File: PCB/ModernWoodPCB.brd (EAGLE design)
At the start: 428.5 x 125 mm, 231 parts, among them Q2 FS8205, U1 ESP32-S3HOLE, U2 ME6211C33M5G

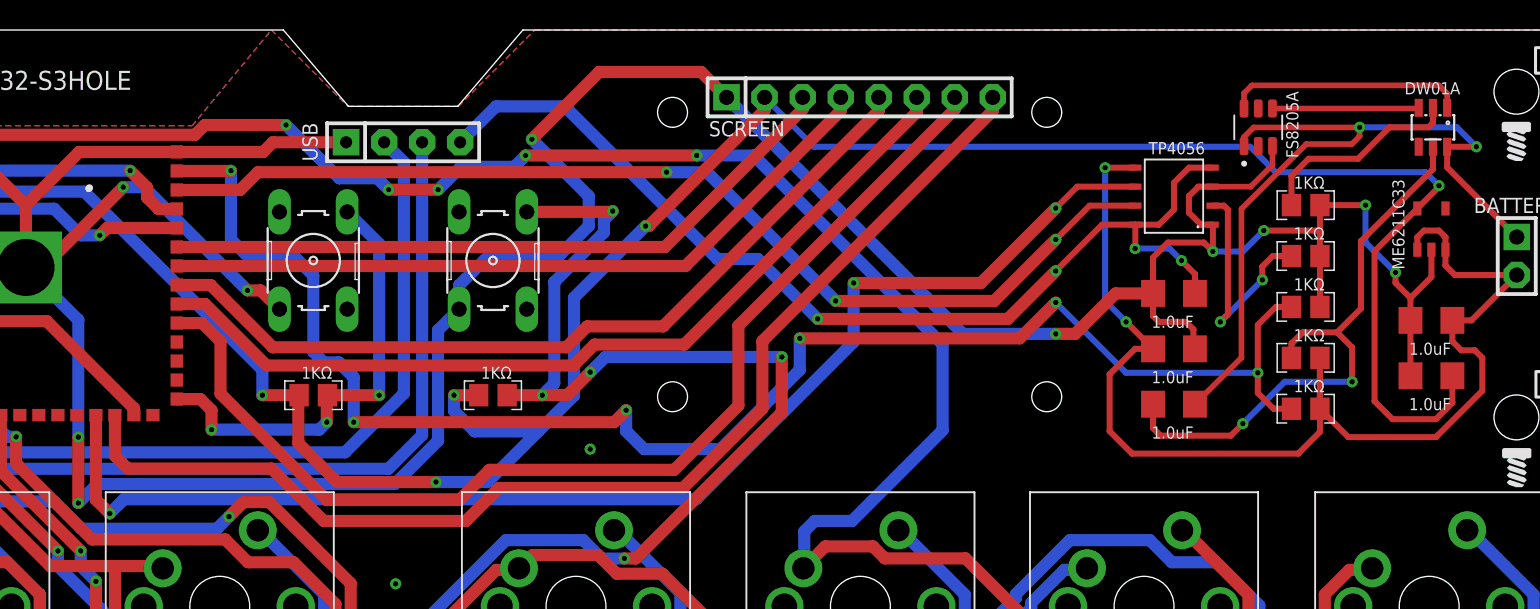
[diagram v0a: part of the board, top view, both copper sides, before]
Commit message: Fixed 5V on Tp4056 status pins
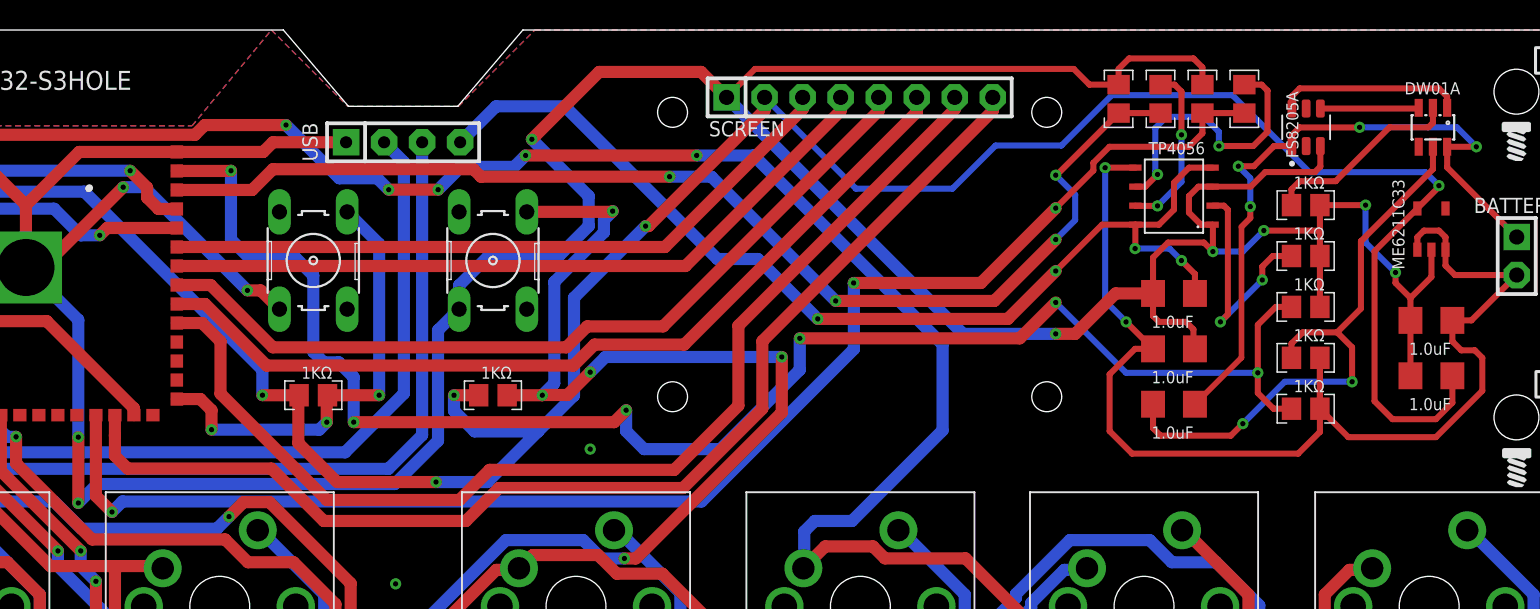
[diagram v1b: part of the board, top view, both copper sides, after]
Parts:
- added R10, R8: 1M, resistors:R-0805
- added R11, R9: 2M, resistors:R-0805
- R6: value 8200000 -> 4M
- moved Q2 3.20 mm to (412.8, 120.5)
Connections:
- new net CHRG_3: R8.2, R9.1, U1.38
- new net STDBY_3: R10.2, R11.1, U1.23
- net CHRG: now also R8.1; no longer U1.38
- net GND: now also R11.2, R9.2
- net STDBY: now also R10.1; no longer U1.23
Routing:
- net STDBY_3: track 0.00 -> 97.3 mm, vias 0 -> 3
- net CHRG_3: track 0.00 -> 78.7 mm, vias 0 -> 4
- net STDBY: track 86.8 -> 19.0 mm, vias 3 -> 2
- net CHRG: track 70.7 -> 11.4 mm, vias 3 -> 2
- net GND: track 676.7 -> 715.8 mm
- net B-: track 51.7 -> 45.6 mm, vias 2 -> 4
- net VCC: track 496.5 -> 501.6 mm
- net N$31: track 16.0 -> 12.4 mm
- net N$32: track 9.79 -> 6.59 mm
- net DWCS: track 13.9 -> 13.3 mm
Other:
- board text removed: "JLCJLCJLCJLC"
